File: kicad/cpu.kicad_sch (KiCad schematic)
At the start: 16 parts, among them U10 74HC00, U13 74HC32, U3 74HC138, U4 W65C02SxP, U5 74HC08, U7 74HC138

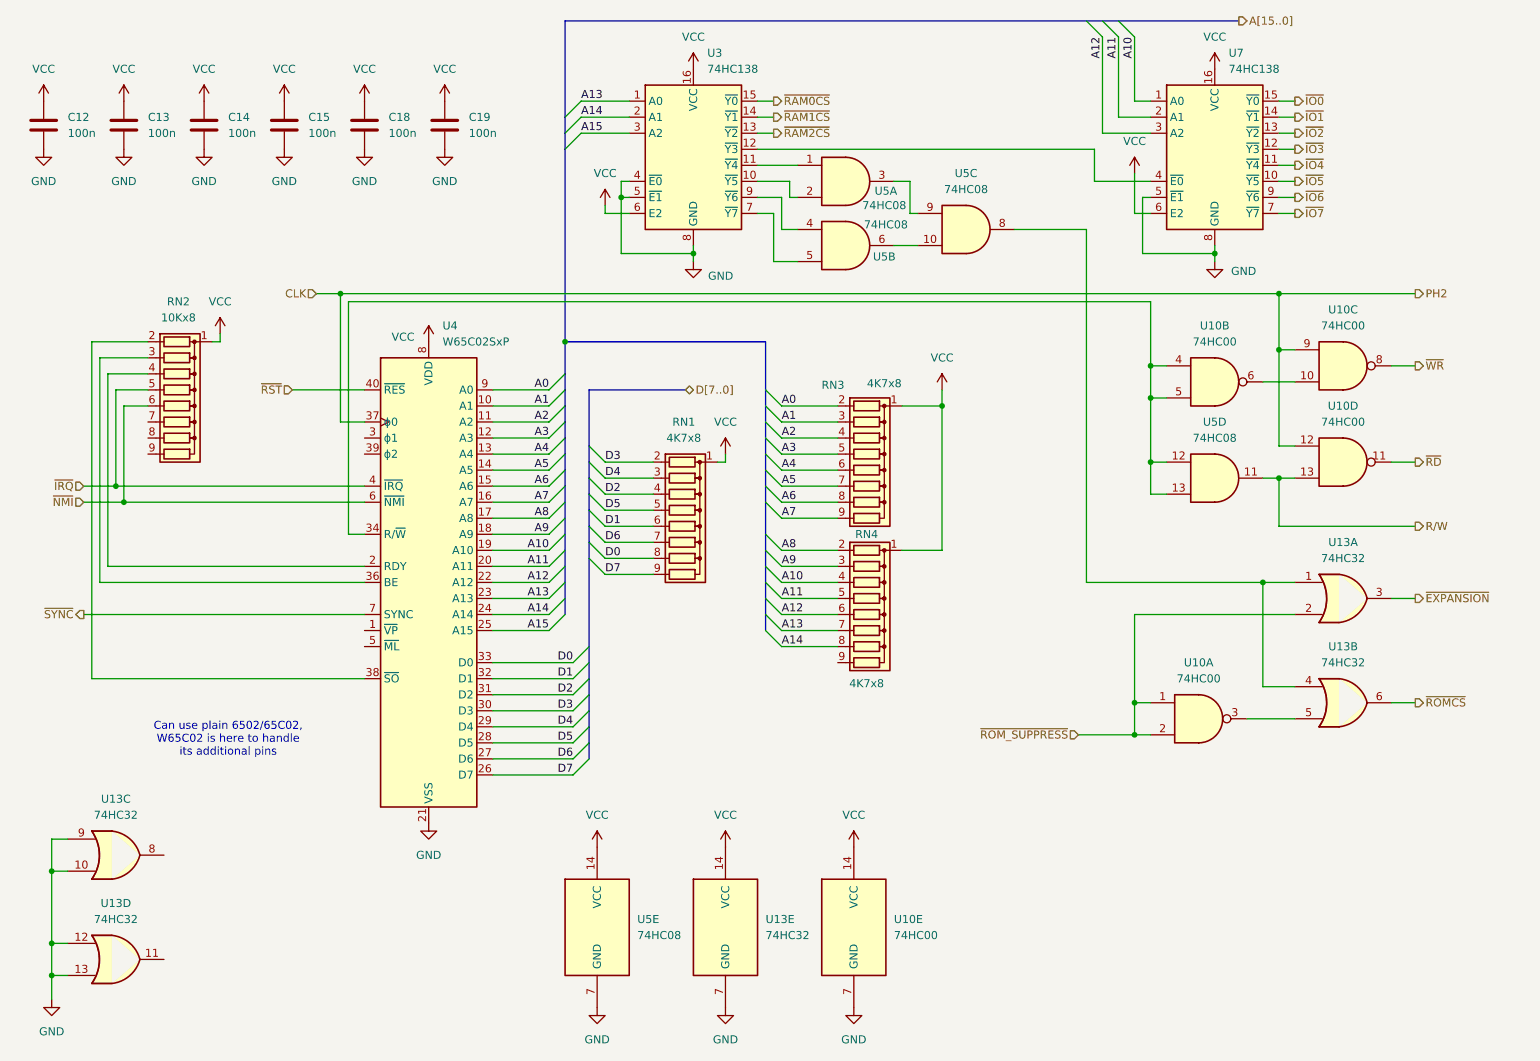
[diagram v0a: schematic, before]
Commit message: hw: rev D - replace DB25 connector footprint with available one
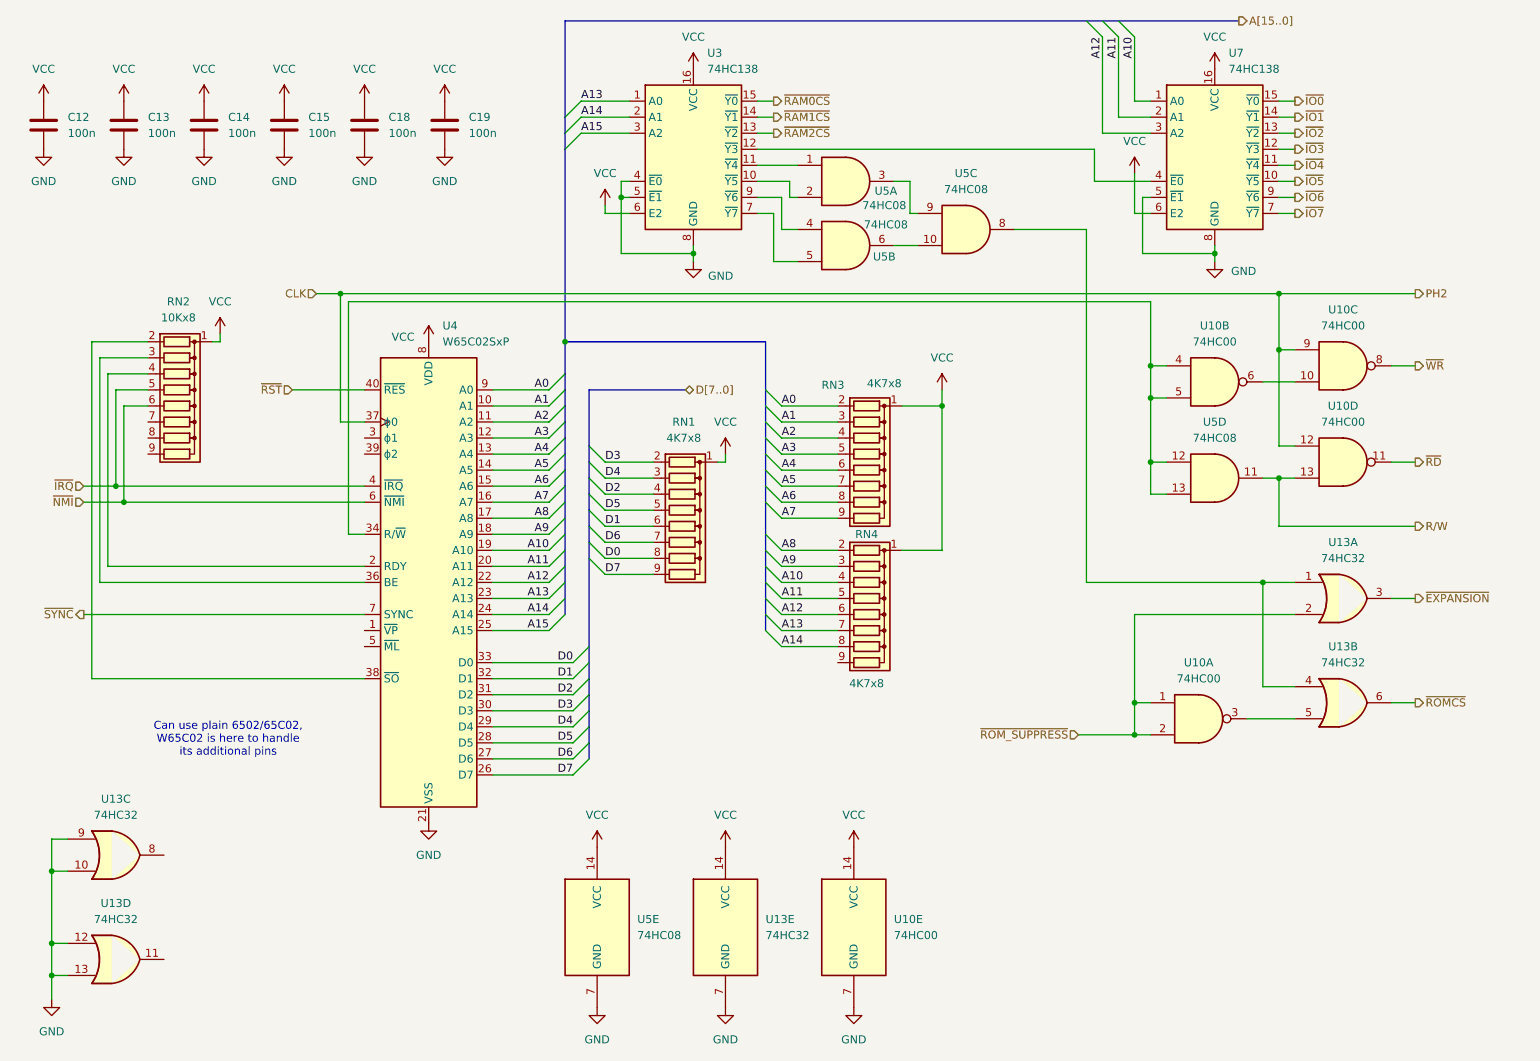
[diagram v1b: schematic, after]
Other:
- company: (none) -> A.K.
- title: (none) -> CPU and memory decoders
